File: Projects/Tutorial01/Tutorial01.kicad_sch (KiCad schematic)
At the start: 0 parts

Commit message: LED with Battery schematic
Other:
- company: (none) -> New Thinking Technologies
- title: (none) -> LED with Battery
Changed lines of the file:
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@@
 	(generator_version "9.0")
 	(paper "A4")
+	(title_block
+		(title "LED with Battery")
+		(date "20251026")
+		(rev "1.00")
+		(company "New Thinking Technologies")
+		(comment 1 "Davide Spano")
+	)
 	(sheet_instances
 		(path "/"

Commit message: added R
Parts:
- added R1: R, symbol Device:R
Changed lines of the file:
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@@
 		(comment 1 "Davide Spano")
+	)
+	(symbol
+		(lib_id "Device:R")
+		(at 83.82 81.28 0)
+		(unit 1)
+		(exclude_from_sim no)
+		(in_bom yes)
+		(on_board yes)
+		(dnp no)
+		(fields_autoplaced yes)
+		(property "Reference" "R1"
+			(at 86.36 80.0099 0)
+			(effects
+				(font
+					(size 1.27 1.27)
+				)
+				(justify left)
+			)
+		)
+		(property "Value" "R"
+			(at 86.36 82.5499 0)
+			(effects
+				(font
+					(size 1.27 1.27)
+				)
+				(justify left)
+			)
+		)
+		(property "Footprint" ""
+			(at 82.042 81.28 90)
+			(effects
+				(font
+					(size 1.27 1.27)
+				)
+				(hide yes)
+			)
+		)
+		(property "Datasheet" "~"
+			(at 83.82 81.28 0)
+			(effects
+				(font
+					(size 1.27 1.27)
+				)
+				(hide yes)
+			)
+		)
+		(property "Description" "Resistor"
+			(at 83.82 81.28 0)
+			(effects
+				(font
+					(size 1.27 1.27)
+				)
+				(hide yes)
+			)
+		)
+		(pin "1"
+		)
+		(pin "2"
+		)
+		(instances
+			(project ""
+				(path "/8ae59741-537a-42c7-8cdd-92d8d9dc48c6"
+					(reference "R1")
+					(unit 1)
+				)
+			)
+		)
 	)
 	(sheet_instances

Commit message: 20251106 diode+battery
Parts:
- added BT1: Battery, symbol Device:Battery
- added D1: LED, symbol Device:LED
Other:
- moved on the sheet: R1
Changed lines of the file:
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@@
 	)
 	(symbol
-		(lib_id "Device:R")
-		(at 83.82 81.28 0)
+		(lib_id "Device:LED")
+		(at 68.58 74.93 180)
 		(unit 1)
 		(exclude_from_sim no)
@@
 		(dnp no)
 		(fields_autoplaced yes)
-		(property "Reference" "R1"
-			(at 86.36 80.0099 0)
+		(property "Reference" "D1"
+			(at 70.1675 67.31 0)
+			(effects
+				(font
+					(size 1.27 1.27)
+				)
+			)
+		)
+		(property "Value" "LED"
+			(at 70.1675 69.85 0)
+			(effects
+				(font
+					(size 1.27 1.27)
+				)
+			)
+		)
+		(property "Footprint" ""
+			(at 68.58 74.93 0)
+			(effects
+				(font
+					(size 1.27 1.27)
+				)
+				(hide yes)
+			)
+		)
+		(property "Datasheet" "~"
+			(at 68.58 74.93 0)
+			(effects
+				(font
+					(size 1.27 1.27)
+				)
+				(hide yes)
+			)
+		)
+		(property "Description" "Light emitting diode"
+			(at 68.58 74.93 0)
+			(effects
+				(font
+					(size 1.27 1.27)
+				)
+				(hide yes)
+			)
+		)
+		(property "Sim.Pins" "1=K 2=A"
+			(at 68.58 74.93 0)
+			(effects
+				(font
+					(size 1.27 1.27)
+				)
+				(hide yes)
+			)
+		)
+		(pin "2"
+		)
+		(pin "1"
+		)
+		(instances
+			(project ""
+				(path "/8ae59741-537a-42c7-8cdd-92d8d9dc48c6"
+					(reference "D1")
+					(unit 1)
+				)
+			)
+		)
+	)
+	(symbol
+		(lib_id "Device:Battery")
+		(at 60.96 83.82 0)
+		(unit 1)
+		(exclude_from_sim no)
+		(in_bom yes)
+		(on_board yes)
+		(dnp no)
+		(fields_autoplaced yes)
+		(property "Reference" "BT1"
+			(at 64.77 81.9784 0)
 			(effects
 				(font
@@
 			)
 		)
-		(property "Value" "R"
-			(at 86.36 82.5499 0)
+		(property "Value" "Battery"
+			(at 64.77 84.5184 0)
 			(effects
 				(font
@@
 		)
 		(property "Footprint" ""
-			(at 82.042 81.28 90)
+			(at 60.96 82.296 90)
 			(effects
 				(font
@@
 		)
 		(property "Datasheet" "~"
-			(at 83.82 81.28 0)
+			(at 60.96 82.296 90)
+			(effects
+				(font
+					(size 1.27 1.27)
+				)
+				(hide yes)
+			)
+		)
+		(property "Description" "Multiple-cell battery"
+			(at 60.96 83.82 0)
+			(effects
+				(font
+					(size 1.27 1.27)
+				)
+				(hide yes)
+			)
+		)
+		(pin "1"
+		)
+		(pin "2"
+		)
+		(instances
+			(project ""
+				(path "/8ae59741-537a-42c7-8cdd-92d8d9dc48c6"
+					(reference "BT1")
+					(unit 1)
+				)
+			)
+		)
+	)
+	(symbol
+		(lib_id "Device:R")
+		(at 80.01 74.93 90)
+		(unit 1)
+		(exclude_from_sim no)
+		(in_bom yes)
+		(on_board yes)
+		(dnp no)
+		(fields_autoplaced yes)
+		(property "Reference" "R1"
+			(at 80.01 68.58 90)
+			(effects
+				(font
+					(size 1.27 1.27)
+				)
+			)
+		)
+		(property "Value" "R"
+			(at 80.01 71.12 90)
+			(effects
+				(font
+					(size 1.27 1.27)
+				)
+			)
+		)
+		(property "Footprint" ""
+			(at 80.01 76.708 90)
+			(effects
+				(font
+					(size 1.27 1.27)
+				)
+				(hide yes)
+			)
+		)
+		(property "Datasheet" "~"
+			(at 80.01 74.93 0)
 			(effects
 				(font
@@
 		)
 		(property "Description" "Resistor"
-			(at 83.82 81.28 0)
+			(at 80.01 74.93 0)
 			(effects
 				(font

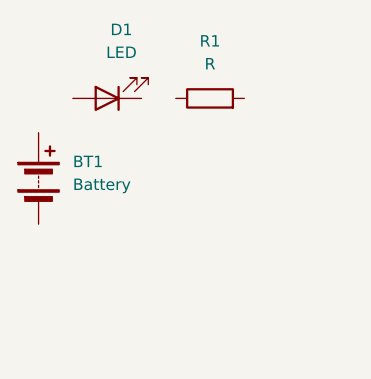
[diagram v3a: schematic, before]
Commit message: 20251108 diode+battery Anschluss
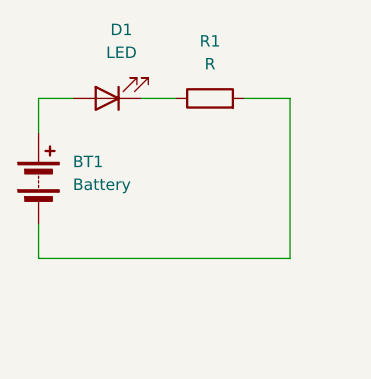
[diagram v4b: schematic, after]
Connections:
- net at D1.1 (K): now also R1.1
- net at D1.2 (A): now also BT1.1 (+)
- net at BT1.2 (-): now also R1.2
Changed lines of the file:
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@@
 		(comment 1 "Davide Spano")
+	)
+	(wire
+		(pts
+			(xy 88.9 92.71) (xy 60.96 92.71)
+		)
+		(stroke
+			(width 0)
+			(type default)
+		)
+	)
+	(wire
+		(pts
+			(xy 83.82 74.93) (xy 88.9 74.93)
+		)
+		(stroke
+			(width 0)
+			(type default)
+		)
+	)
+	(wire
+		(pts
+			(xy 88.9 74.93) (xy 88.9 92.71)
+		)
+		(stroke
+			(width 0)
+			(type default)
+		)
+	)
+	(wire
+		(pts
+			(xy 60.96 78.74) (xy 60.96 74.93)
+		)
+		(stroke
+			(width 0)
+			(type default)
+		)
+	)
+	(wire
+		(pts
+			(xy 72.39 74.93) (xy 76.2 74.93)
+		)
+		(stroke
+			(width 0)
+			(type default)
+		)
+	)
+	(wire
+		(pts
+			(xy 60.96 92.71) (xy 60.96 88.9)
+		)
+		(stroke
+			(width 0)
+			(type default)
+		)
+	)
+	(wire
+		(pts
+			(xy 60.96 74.93) (xy 64.77 74.93)
+		)
+		(stroke
+			(width 0)
+			(type default)
+		)
 	)
 	(symbol

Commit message: 20251108 Schaltplan mit Batterie 9V, eine rote Diode 3 mm Durchmnesser und ein Widerstand 220 ohm
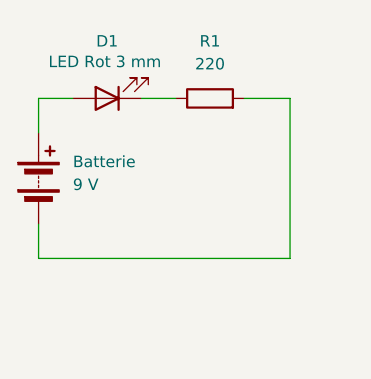
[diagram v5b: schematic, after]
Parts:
- Batterie: renamed from BT1; value Battery -> 9 V
- D1: value LED -> LED Rot 3 mm
- R1: value R -> 220
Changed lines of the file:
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@@
 		(on_board yes)
 		(dnp no)
-		(fields_autoplaced yes)
 		(property "Reference" "D1"
-			(at 70.1675 67.31 0)
+			(at 68.58 68.58 0)
 			(effects
 				(font
@@
 			)
 		)
-		(property "Value" "LED"
-			(at 70.1675 69.85 0)
+		(property "Value" "LED Rot 3 mm"
+			(at 68.326 70.866 0)
 			(effects
 				(font
@@
 		(dnp no)
 		(fields_autoplaced yes)
-		(property "Reference" "BT1"
+		(property "Reference" "Batterie"
 			(at 64.77 81.9784 0)
 			(effects
@@
 			)
 		)
-		(property "Value" "Battery"
+		(property "Value" "9 V"
 			(at 64.77 84.5184 0)
 			(effects
@@
 			(project ""
 				(path "/8ae59741-537a-42c7-8cdd-92d8d9dc48c6"
-					(reference "BT1")
+					(reference "Batterie")
 					(unit 1)
 				)
@@
 			)
 		)
-		(property "Value" "R"
+		(property "Value" "220"
 			(at 80.01 71.12 90)
 			(effects

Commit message: 20251108 Schaltplan mit Batterie 9V, eine rote Diode 3 mm Durchmnesser und ein Widerstand 220 ohm
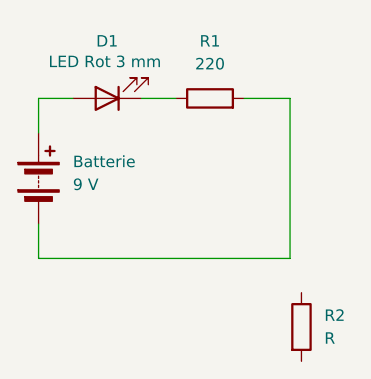
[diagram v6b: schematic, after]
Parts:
- added R2: R, symbol Device:R
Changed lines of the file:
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@@
+		)
+	)
+	(symbol
+		(lib_id "Device:R")
+		(at 90.17 100.33 0)
+		(unit 1)
+		(exclude_from_sim no)
+		(in_bom yes)
+		(on_board yes)
+		(dnp no)
+		(fields_autoplaced yes)
+		(property "Reference" "R2"
+			(at 92.71 99.0599 0)
+			(effects
+				(font
+					(size 1.27 1.27)
+				)
+				(justify left)
+			)
+		)
+		(property "Value" "R"
+			(at 92.71 101.5999 0)
+			(effects
+				(font
+					(size 1.27 1.27)
+				)
+				(justify left)
+			)
+		)
+		(property "Footprint" ""
+			(at 88.392 100.33 90)
+			(effects
+				(font
+					(size 1.27 1.27)
+				)
+				(hide yes)
+			)
+		)
+		(property "Datasheet" "~"
+			(at 90.17 100.33 0)
+			(effects
+				(font
+					(size 1.27 1.27)
+				)
+				(hide yes)
+			)
+		)
+		(property "Description" "Resistor"
+			(at 90.17 100.33 0)
+			(effects
+				(font
+					(size 1.27 1.27)
+				)
+				(hide yes)
+			)
+		)
+		(pin "1"
+		)
+		(pin "2"
+		)
+		(instances
+			(project ""
+				(path "/8ae59741-537a-42c7-8cdd-92d8d9dc48c6"
+					(reference "R2")
+					(unit 1)
+				)
+			)
 		)
 	)

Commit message: 20251110 diode+battery referenze und ERC
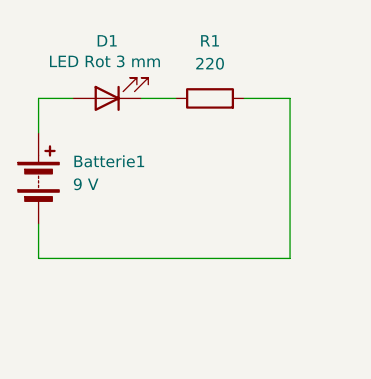
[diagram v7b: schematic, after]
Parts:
- removed R2: R, symbol Device:R
- renumbered Batterie to Batterie1
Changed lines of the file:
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@@
 		(dnp no)
 		(fields_autoplaced yes)
-		(property "Reference" "Batterie"
+		(property "Reference" "Batterie1"
 			(at 64.77 81.9784 0)
 			(effects
@@
 			(project ""
 				(path "/8ae59741-537a-42c7-8cdd-92d8d9dc48c6"
-					(reference "Batterie")
+					(reference "Batterie1")
 					(unit 1)
 				)
@@
 					(unit 1)
 				)
-			)
-		)
-	)
-	(symbol
-		(lib_id "Device:R")
-		(at 90.17 100.33 0)
-		(unit 1)
-		(exclude_from_sim no)
-		(in_bom yes)
-		(on_board yes)
-		(dnp no)
-		(fields_autoplaced yes)
-		(property "Reference" "R2"
-			(at 92.71 99.0599 0)
-			(effects
-				(font
-					(size 1.27 1.27)
-				)
-				(justify left)
-			)
-		)
-		(property "Value" "R"
-			(at 92.71 101.5999 0)
-			(effects
-				(font
-					(size 1.27 1.27)
-				)
-				(justify left)
-			)
-		)
-		(property "Footprint" ""
-			(at 88.392 100.33 90)
-			(effects
-				(font
-					(size 1.27 1.27)
-				)
-				(hide yes)
-			)
-		)
-		(property "Datasheet" "~"
-			(at 90.17 100.33 0)
-			(effects
-				(font
-					(size 1.27 1.27)
-				)
-				(hide yes)
-			)
-		)
-		(property "Description" "Resistor"
-			(at 90.17 100.33 0)
-			(effects
-				(font
-					(size 1.27 1.27)
-				)
-				(hide yes)
-			)
-		)
-		(pin "1"
-		)
-		(pin "2"
-		)
-		(instances
-			(project ""
-				(path "/8ae59741-537a-42c7-8cdd-92d8d9dc48c6"
-					(reference "R2")
-					(unit 1)
-				)
